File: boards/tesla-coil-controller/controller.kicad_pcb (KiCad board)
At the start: 2 copper layers, 163 x 141.8 mm, 331 parts, among them J1 DF40C-40DP-0.4V(51), J10 AUX 4 / 0-5V, J2 DF40C(2.0)-40DS-0.4V(51), J3 AUX 1 / 0-5V, J30 12V BATTERY / LOWER, J4 12V BATTERY / UPPER, J40 CST SECONDARY, J5 USB-C / PROGRAMMING ONLY, J50 GDT 1 PRIMARY, J51 GDT 2 PRIMARY, J60 CST 2 SECONDARY, J8 AUX 2 / 0-5V, J9 AUX 3 / 0-5V, Q50 STD80N10F7, Q51 STD80N10F7, Q52 STD80N10F7, Q53 STD80N10F7, Q54 STD80N10F7, Q55 STD80N10F7, Q56 STD80N10F7, Q57 STD80N10F7, U1 AD7606C-16BSTZ, U2 AP2112K-3.3, U3 USBLC6-2SC6, U30 LMZ14202HTZX/NOPB, U31 LMZ14202HTZX/NOPB, U40 OPA197IDBVR, U41 OPA197IDBVR, U42 TLV3501AIDBVR, U44 TPS60403DBVR, U51 UCC27282DR, U52 UCC27282DR, U53 UCC27282DR, U54 UCC27282DR, U60 OPA197IDBVR, U61 OPA197IDBVR, U62 TLV3501AIDBVR, U70 OPA197IDBVR, U71 OPA197IDBVR, U72 OPA197IDBVR, U73 OPA197IDBVR

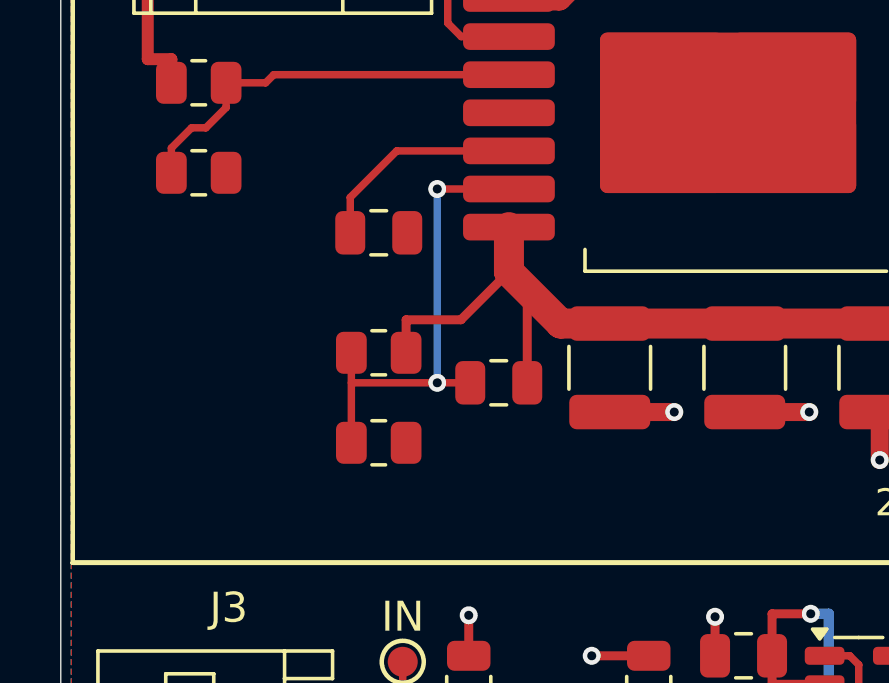
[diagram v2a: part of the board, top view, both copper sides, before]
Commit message: Stack the U30 feedback divider under pin 6 so P30_FB stays on F.Cu
Portal edit-stack item: "Rearrange passives so underneath trace is
unneeded". P30_FB left U30 pin 6, dropped to B.Cu at (32.95,64.54), ran
6.5 mm under the +12V_BIAS feed to R300 and resurfaced at the divider.
The crossing was forced by R300/R301 sitting left of the +12V feed with
their FB pads on the far side.

R300 (34k), C301 (22nF) and R301 (2.43k) now form a column at x=33.9
directly below pin 6 (y 70.0 / 72.1 / 74.2), with every FB pad on the
x=33.0 line and every +12V pad on the right. P30_FB is one F.Cu run:
straight out of pin 6, one 45° bend, then down through the three FB pads.
+12V_BIAS taps the divider from a 0.3 mm vertical at x=35.95 off the
existing 1.0 mm diagonal, which replaces the 0.3 mm stub that previously
teed into the 1.0 mm corner at (35.34,67.3). R301's GND pad is zone-fed
as before. Both vias and the B.Cu segment are gone.

Generator-owned: tesla_placement.json and tesla_reviewed_routing.json
edited and replayed. Only R300/C301/R301 moved; only P30_FB and
+12V_BIAS copper changed. DRC 0/0/0 (kicad-cli and kicadmium). kct lint:
0 open, no new findings; the four width.taper / trace.width_transition
findings at (35.34,67.3) are resolved and their exceptions removed.
Evidence refreshed for the remaining 184 (128 ignored, 56 flagged).

Co-Authored-By: Claude Fable 5.1 <noreply@anthropic.com>
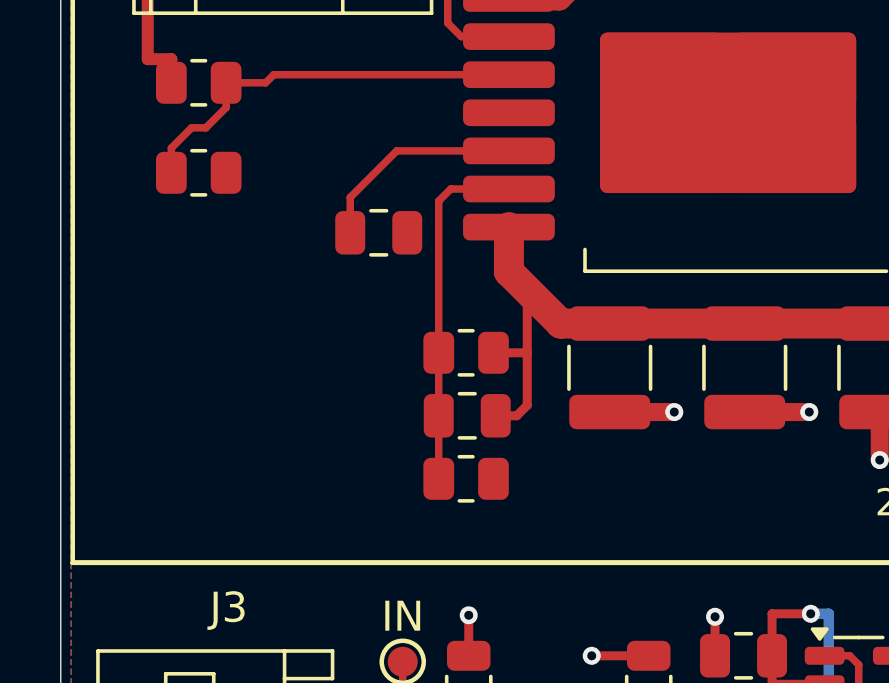
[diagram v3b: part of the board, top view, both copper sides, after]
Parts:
- moved R301 3.15 mm to (33.9, 74.2)
- moved R300 2.91 mm to (33.9, 70.0)
- moved C301 1.52 mm to (34.0, 72.1)
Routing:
- net P30_FB: track 15.8 -> 11.8 mm, vias 2 -> 0
- net +12V_BIAS: track 280.0 -> 277.9 mm
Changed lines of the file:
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@@
 	(footprint "Tesla:R_0805_2012Metric"
 		(layer "F.Cu")
-		(at 31 73)
+		(at 33.9125 74.2)
 		(descr "Resistor SMD 0805 (2012 Metric), square (rectangular) end terminal, IPC_7351 nominal, (Body size source: IPC-SM-782 page 72, https://www.pcb-3d.com/wordpress/wp-content/uploads/ipc-sm-782a_amendment_1_and_2.pdf), generated with kicad-footprint-generator")
 		(tags "resistor")
 		(property "Reference" "R301"
-			(at 0 -5 0)
+			(at -2.3125 0 0)
 			(layer "F.SilkS")
 			(hide yes)
@@
 	(footprint "Tesla:C_0805_2012Metric"
 		(layer "F.Cu")
-		(at 35 71 180)
+		(at 33.95 72.1 180)
 		(descr "Capacitor SMD 0805 (2012 Metric), square (rectangular) end terminal, IPC_7351 nominal, (Body size source: IPC-SM-782 page 76, https://www.pcb-3d.com/wordpress/wp-content/uploads/ipc-sm-782a_amendment_1_and_2.pdf, https://docs.google.com/spreadsheets/d/1BsfQQcO9C6DZCsRaXUlFlo91Tg2WpOkGARC1WS5S8t0/edit?usp=sharing), generated with kicad-footprint-generator")
 		(tags "capacitor")
 		(property "Reference" "C301"
-			(at 0 5 180)
+			(at 2.35 0 180)
 			(layer "F.SilkS")
 			(hide yes)
@@
 	(footprint "Tesla:R_0805_2012Metric"
 		(layer "F.Cu")
-		(at 31 70 180)
+		(at 33.9125 70 180)
 		(descr "Resistor SMD 0805 (2012 Metric), square (rectangular) end terminal, IPC_7351 nominal, (Body size source: IPC-SM-782 page 72, https://www.pcb-3d.com/wordpress/wp-content/uploads/ipc-sm-782a_amendment_1_and_2.pdf), generated with kicad-footprint-generator")
 		(tags "resistor")
 		(property "Reference" "R300"
-			(at 0 5 180)
+			(at 2.3125 0 180)
 			(layer "F.SilkS")
 			(hide yes)
@@
 	)
 	(segment
-		(start 31.9125 68.9)
-		(end 33.74 68.9)
+		(start 35.95 67.91)
+		(end 35.95 71.75)
+		(width 0.3)
+		(layer "F.Cu")
+		(net "+12V_BIAS")
+	)
+	(segment
+		(start 35.95 71.75)
+		(end 35.6 72.1)
+		(width 0.3)
+		(layer "F.Cu")
+		(net "+12V_BIAS")
+	)
+	(segment
+		(start 35.6 72.1)
+		(end 34.9 72.1)
+		(width 0.3)
+		(layer "F.Cu")
+		(net "+12V_BIAS")
+	)
+	(segment
+		(start 35.95 70)
+		(end 34.825 70)
 		(width 0.3)
 		(layer "F.Cu")
@@
 	)
 	(segment
-		(start 33.74 68.9)
-		(end 35.34 67.3)
-		(width 0.3)
-		(layer "F.Cu")
-		(net "+12V_BIAS")
-	)
-	(segment
 		(start 155.8 122.5)
 		(end 154.2 122.5)
@@
 	)
 	(segment
-		(start 35.95 71)
-		(end 35.95 67.91)
-		(width 0.3)
-		(layer "F.Cu")
-		(net "+12V_BIAS")
-	)
-	(segment
 		(start 137.8 126.025)
 		(end 137.8 122.5)
@@
 		(net "+12V_BIAS")
 	)
-	(segment
-		(start 31.9125 70)
-		(end 31.9125 68.9)
-		(width 0.3)
-		(layer "F.Cu")
-		(net "+12V_BIAS")
-	)
 	(via
 		(at 154.2 122.5)
@@
 	(segment
 		(start 35.34 64.54)
-		(end 32.95 64.54)
+		(end 33.4 64.54)
 		(width 0.25)
 		(layer "F.Cu")
@@
 	)
 	(segment
-		(start 30.0875 71)
-		(end 34.05 71)
+		(start 33.4 64.54)
+		(end 33 64.94)
 		(width 0.25)
 		(layer "F.Cu")
@@
 	)
 	(segment
-		(start 30.0875 70)
-		(end 30.0875 73)
+		(start 33 64.94)
+		(end 33 74.2)
 		(width 0.25)
 		(layer "F.Cu")
 		(net "P30_FB")
 	)
-	(via
-		(at 32.95 71)
-		(size 0.6)
-		(drill 0.3)
-		(layers "F.Cu" "B.Cu")
-		(net "P30_FB")
-	)
-	(via
-		(at 32.95 64.54)
-		(size 0.6)
-		(drill 0.3)
-		(layers "F.Cu" "B.Cu")
-		(net "P30_FB")
-	)
-	(segment
-		(start 32.95 64.54)
-		(end 32.95 71)
-		(width 0.25)
-		(layer "B.Cu")
-		(net "P30_FB")
-	)

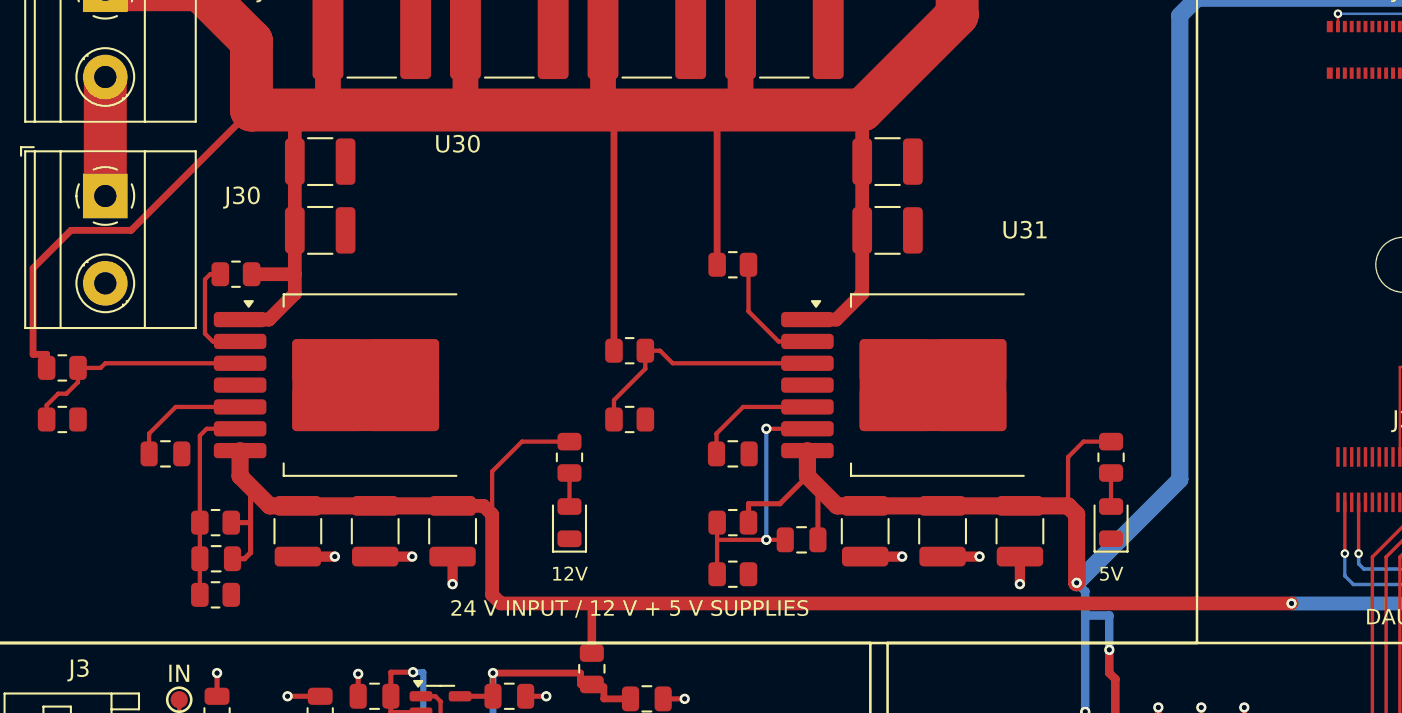
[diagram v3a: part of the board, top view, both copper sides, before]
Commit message: Shift U30 right 4 mm so its passives sit like U31's, clear of J30
Portal edit-stack item: "scooch this regulator a bit to the right and
make it and its sister have roughly the same layout, not congested by the
input pins". U31 keeps its RON resistor at (-12,-7) from the module and
its soft-start cap at (-12,4); U30 could not, because J30's courtyard
reaches x=33.3 and sat 0.25 mm from U30's left pin column, so R302 and
the feedback column were wedged against the pins.

U30 moves from (43,62) to (47,62) together with its own parts: C302/C303
input caps, C304/C305/C306 output caps, C300 soft-start cap and the
R300/C301/R301 feedback column. R302 now stands vertically at (37,54.75)
in the opened slot beside the pins, VBAT pad up, fed by a 0.4 mm tee off
the 2.5 mm VBAT bus at x=37 (the same arrangement as U31's R312), with
RON running down x=37 and entering pin 2 straight. All P30_* copper, the
VBAT trunk to pin 1, the +12V run to the output caps and the GND via
stubs translate with the group; the UVLO lead to pin 3 just lengthens.

The +12V drop to the y=74.7 bus previously sat at x=50, where C306 now
lands. It is now a tee off the 1.0 mm run between C305 and C306 at
x=49.45, and C305's GND via moves below its pad to vacate that gap. The
R801 LED feed enters C306's +12V pad from above instead of the drop.

U31 is untouched. Its feedback divider still uses the B.Cu jumper that
was removed from U30 in fccb755; restacking it the same way is a
separate change.

Generator-owned: tesla_placement.json and tesla_reviewed_routing.json
edited and replayed. DRC 0/0/0 (kicad-cli and kicadmium). kct lint:
0 open, no new findings; six findings at the old drop corner (50,69.525)
and (47.7,69.025) are resolved and their exceptions removed. Evidence
refreshed for the remaining 178 (122 ignored, 56 flagged).

Co-Authored-By: Claude Fable 5.1 <noreply@anthropic.com>
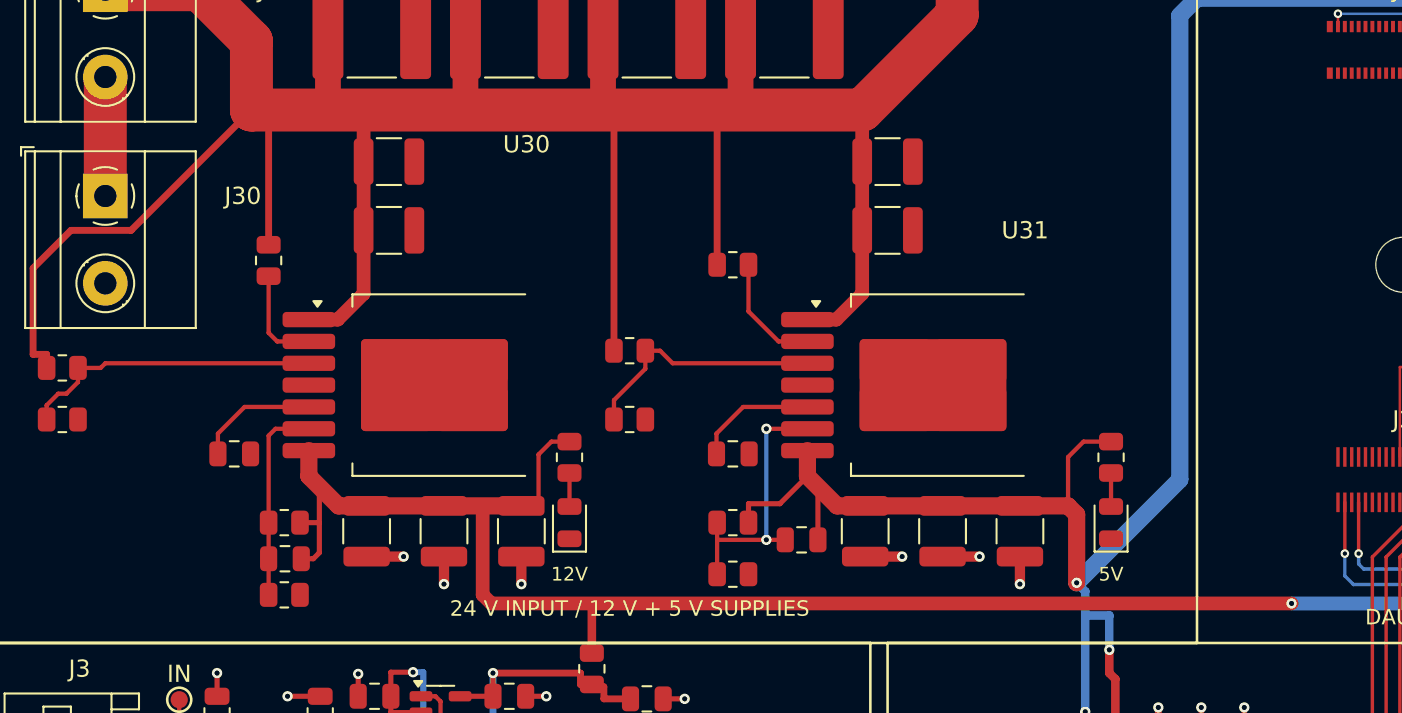
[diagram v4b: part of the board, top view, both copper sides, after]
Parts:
- moved C300 4.00 mm to (35.0, 66.0)
- moved C301 4.00 mm to (38.0, 72.1)
- moved C302 4.00 mm to (44.0, 53.0)
- moved C303 4.00 mm to (44.0, 49.0)
- moved C304 4.00 mm to (42.7, 70.5)
- moved C305 4.00 mm to (47.2, 70.5)
- moved C306 4.00 mm to (51.7, 70.5)
- moved R300 4.00 mm to (37.9, 70.0)
- moved R301 4.00 mm to (37.9, 74.2)
- moved U30 4.00 mm to (47.0, 62.0)
- moved R302 2.06 mm to (37.0, 54.8), turned to -90 degrees
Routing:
- net VBAT_24V: track 604.3 -> 609.7 mm
- net +12V_BIAS: track 277.9 -> 273.4 mm
- net P30_UVLO: track 13.6 -> 17.6 mm
- net P30_RON: track 6.40 -> 5.84 mm
- net GND: track 365.4 -> 364.9 mm
